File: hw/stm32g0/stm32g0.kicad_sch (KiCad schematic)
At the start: 11 parts, among them J101 Barrel_Jack_Switch, J102 Screw_Terminal_01x03, Q101 BC817

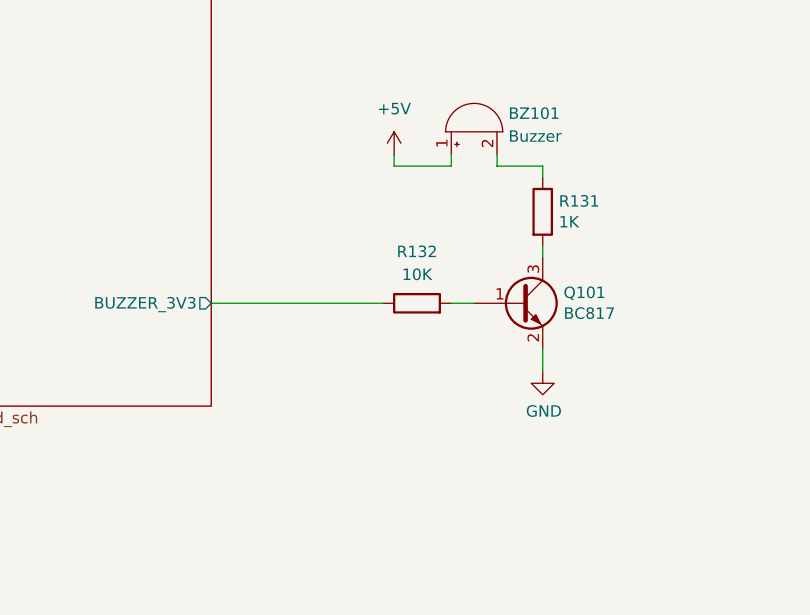
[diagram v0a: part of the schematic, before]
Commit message: chore(hw): minor layout and schematic improvements
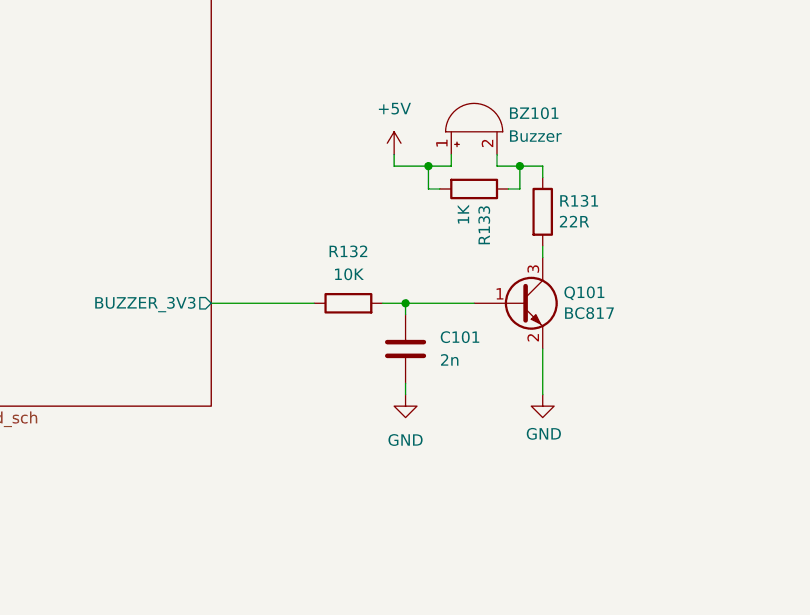
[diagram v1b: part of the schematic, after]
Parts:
- added C101: 2n, Capacitor_SMD:C_0805_2012Metric_Pad1.18x1.45mm_HandSolder, symbol Device:C
- added R133: 1K, Resistor_SMD:R_0805_2012Metric_Pad1.20x1.40mm_HandSolder, symbol Device:R
- R131: value 1K -> 22R
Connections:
- net +5V: now also R133.2
- net GND: now also C101.2
- net at Q101.1 (B), R132.2: now also C101.1
- net at BZ101.2 (-), R131.1: now also R133.1
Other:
- moved on the sheet: R132

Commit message: chore(hw): update title blocks
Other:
- title: ATtiny85 LED Controller -> STM32G0 LED Controller
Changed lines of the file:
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@@
 	(paper "A4")
 	(title_block
-		(title "ATtiny85 LED Controller")
-		(date "2024-01-01")
+		(title "STM32G0 LED Controller")
+		(date "2024-06-29")
 		(company "Stefan Misik")
 		(comment 1 "www.stefanmisik.com")

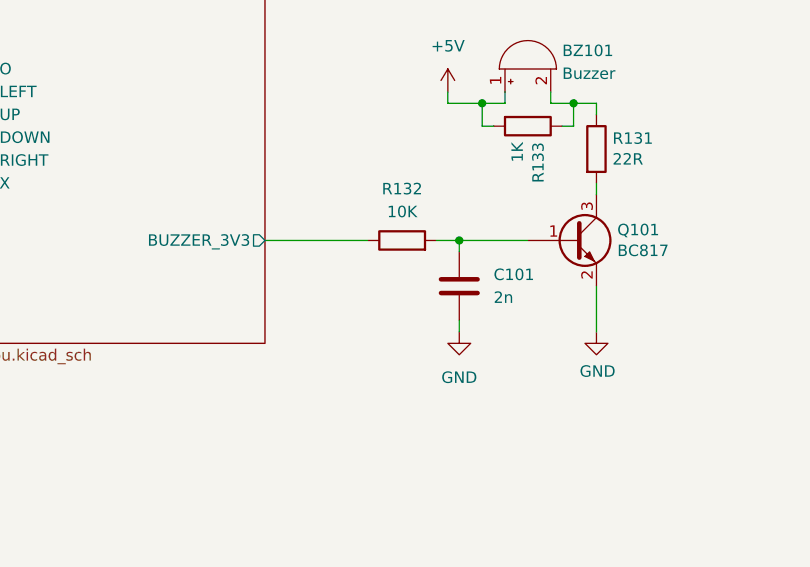
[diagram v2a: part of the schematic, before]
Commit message: chore(hw): remove unnecessary buzzer capacitor
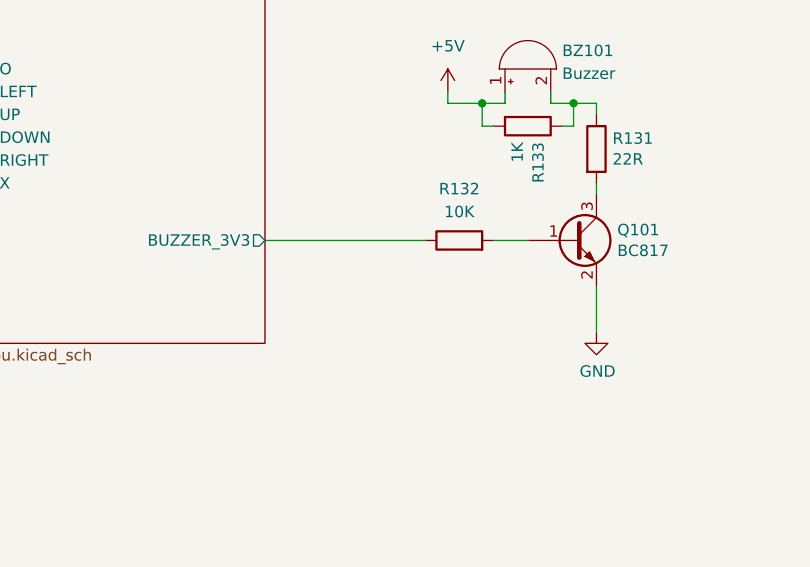
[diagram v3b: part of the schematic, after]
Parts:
- removed C101: 2n, Capacitor_SMD:C_0805_2012Metric_Pad1.18x1.45mm_HandSolder, symbol Device:C
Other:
- moved on the sheet: R132
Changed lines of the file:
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@@
-	)
-	(junction
-		(at 186.69 120.65)
-		(diameter 0)
-		(color 0 0 0 0)
 	)
 	(junction
@@
 	(wire
 		(pts
-			(xy 165.1 120.65) (xy 176.53 120.65)
+			(xy 165.1 120.65) (xy 182.88 120.65)
 		)
 		(stroke
@@
 	(wire
 		(pts
-			(xy 186.69 120.65) (xy 194.31 120.65)
+			(xy 190.5 120.65) (xy 194.31 120.65)
 		)
 		(stroke
@@
 	(wire
 		(pts
-			(xy 184.15 120.65) (xy 186.69 120.65)
-		)
-		(stroke
-			(width 0)
-			(type default)
-		)
-	)
-	(wire
-		(pts
 			(xy 186.69 57.15) (xy 193.04 57.15)
 		)
@@
 	(wire
 		(pts
-			(xy 186.69 120.65) (xy 186.69 121.92)
-		)
-		(stroke
-			(width 0)
-			(type default)
-		)
-	)
-	(wire
-		(pts
 			(xy 196.85 104.14) (xy 196.85 105.41)
 		)
@@
 		(pts
 			(xy 68.58 195.58) (xy 68.58 179.07)
-		)
-		(stroke
-			(width 0)
-			(type default)
-		)
-	)
-	(wire
-		(pts
-			(xy 186.69 129.54) (xy 186.69 130.81)
 		)
 		(stroke
@@
 	)
 	(symbol
-		(lib_id "power:GND")
-		(at 186.69 130.81 0)
-		(unit 1)
-		(exclude_from_sim no)
-		(in_bom yes)
-		(on_board yes)
-		(dnp no)
-		(fields_autoplaced yes)
-		(property "Reference" "#PWR06"
-			(at 186.69 137.16 0)
-			(effects
-				(font
-					(size 1.27 1.27)
-				)
-				(hide yes)
-			)
-		)
-		(property "Value" "GND"
-			(at 186.69 135.89 0)
-			(effects
-				(font
-					(size 1.27 1.27)
-				)
-			)
-		)
-		(property "Footprint" ""
-			(at 186.69 130.81 0)
-			(effects
-				(font
-					(size 1.27 1.27)
-				)
-				(hide yes)
-			)
-		)
-		(property "Datasheet" ""
-			(at 186.69 130.81 0)
-			(effects
-				(font
-					(size 1.27 1.27)
-				)
-				(hide yes)
-			)
-		)
-		(property "Description" "Power symbol creates a global label with name \"GND\" , ground"
-			(at 186.69 130.81 0)
-			(effects
-				(font
-					(size 1.27 1.27)
-				)
-				(hide yes)
-			)
-		)
-		(pin "1"
-		)
-		(instances
-			(project "stm32g0"
-				(path "/fc4ba96f-a9f8-4f1a-a9c5-2b16679a6770"
-					(reference "#PWR06")
-					(unit 1)
-				)
-			)
-		)
-	)
-	(symbol
 		(lib_id "Device:R")
 		(at 201.93 110.49 0)
@@
 	(symbol
 		(lib_id "Device:R")
-		(at 180.34 120.65 90)
+		(at 186.69 120.65 90)
 		(unit 1)
 		(exclude_from_sim no)
@@
 		(dnp no)
 		(property "Reference" "R132"
-			(at 180.34 114.935 90)
+			(at 186.69 114.935 90)
 			(effects
 				(font
@@
 		)
 		(property "Value" "10K"
-			(at 180.34 117.475 90)
+			(at 186.69 117.475 90)
 			(effects
 				(font
@@
 		)
 		(property "Footprint" "Resistor_SMD:R_0805_2012Metric_Pad1.20x1.40mm_HandSolder"
-			(at 180.34 122.428 90)
+			(at 186.69 122.428 90)
 			(effects
 				(font
@@
 		)
 		(property "Datasheet" "~"
-			(at 180.34 120.65 0)
+			(at 186.69 120.65 0)
 			(effects
 				(font
@@
 		)
 		(property "Description" "Resistor"
-			(at 180.34 120.65 0)
+			(at 186.69 120.65 0)
 			(effects
 				(font
@@
 					(unit 1)
 				)
-			)
-		)
-	)
-	(symbol
-		(lib_id "Device:C")
-		(at 186.69 125.73 0)
-		(unit 1)
-		(exclude_from_sim no)
-		(in_bom yes)
-		(on_board yes)
-		(dnp no)
-		(fields_autoplaced yes)
-		(property "Reference" "C101"
-			(at 190.5 124.4599 0)
-			(effects
-				(font
-					(size 1.27 1.27)
-				)
-				(justify left)
-			)
-		)
-		(property "Value" "2n"
-			(at 190.5 126.9999 0)
-			(effects
-				(font
-					(size 1.27 1.27)
-				)
-				(justify left)
-			)
-		)
-		(property "Footprint" "Capacitor_SMD:C_0805_2012Metric_Pad1.18x1.45mm_HandSolder"
-			(at 187.6552 129.54 0)
-			(effects
-				(font
-					(size 1.27 1.27)
-				)
-				(hide yes)
-			)
-		)
-		(property "Datasheet" "~"
-			(at 186.69 125.73 0)
-			(effects
-				(font
-					(size 1.27 1.27)
-				)
-				(hide yes)
-			)
-		)
-		(property "Description" "Unpolarized capacitor"
-			(at 186.69 125.73 0)
-			(effects
-				(font
-					(size 1.27 1.27)
-				)
-				(hide yes)
-			)
-		)
-		(pin "2"
-		)
-		(pin "1"
-		)
-		(instances
-			(project "stm32g0"
-				(path "/fc4ba96f-a9f8-4f1a-a9c5-2b16679a6770"
-					(reference "C101")
-					(unit 1)
-				)

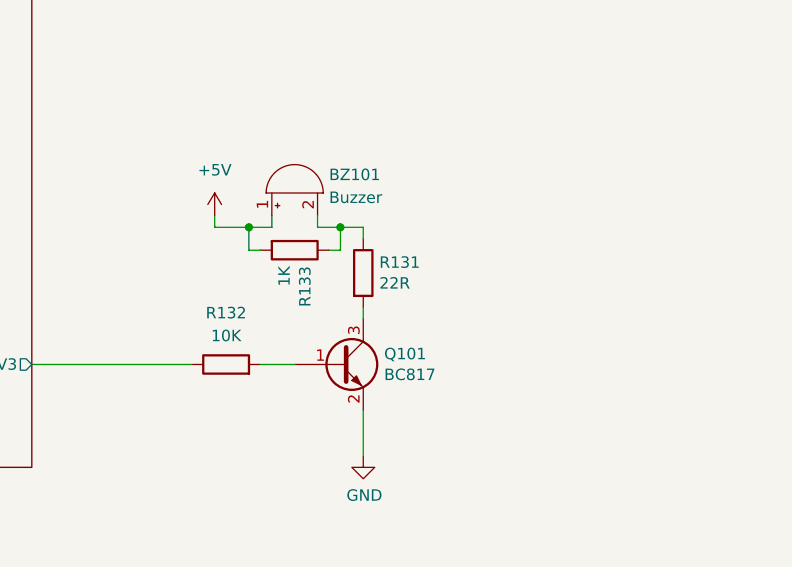
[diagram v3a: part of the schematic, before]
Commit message: chore(hw): change value of buzzer resistor
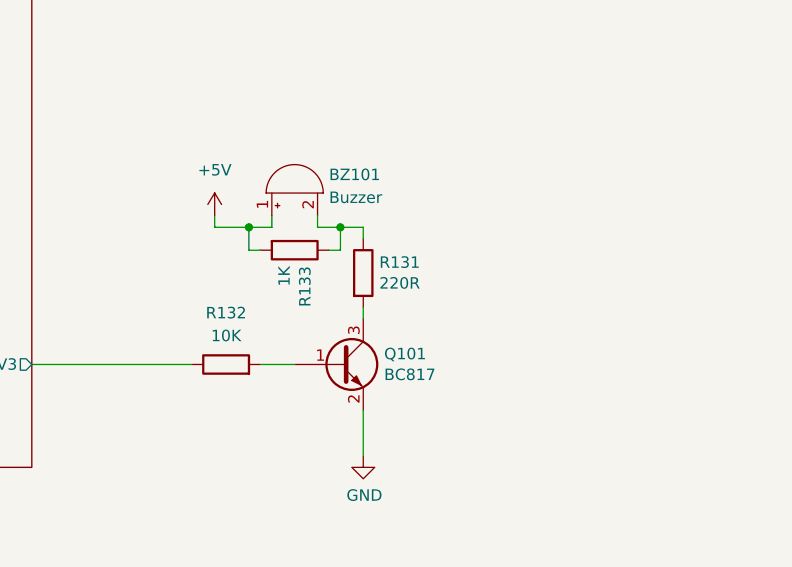
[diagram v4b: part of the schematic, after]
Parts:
- R131: value 22R -> 220R
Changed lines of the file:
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@@
 			)
 		)
-		(property "Value" "22R"
+		(property "Value" "220R"
 			(at 203.708 111.633 0)
 			(effects

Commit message: chore(hw): general improvements, utilize some unused CPU pins
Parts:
- D101: footprint Package_TO_SOT_SMD:SOT-23 -> Package_TO_SOT_SMD:SOT-23_Handsoldering
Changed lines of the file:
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@@
 			)
 		)
-		(property "Footprint" "Package_TO_SOT_SMD:SOT-23"
+		(property "Footprint" "Package_TO_SOT_SMD:SOT-23_Handsoldering"
 			(at 202.565 53.975 0)
 			(effects
